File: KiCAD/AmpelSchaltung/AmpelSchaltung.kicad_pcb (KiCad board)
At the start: 2 copper layers, 100 x 100 mm, 31 parts, among them J1 PWR, J2 usb, J3 Conn_01x06_Pin, J5 Conn_01x04_Pin, J6 Conn_01x08_Pin, SW3 SW_SPDT, SW4 SW_SPDT, U1 74HC00, U2 74HC00, U3 AMS1117-3.3

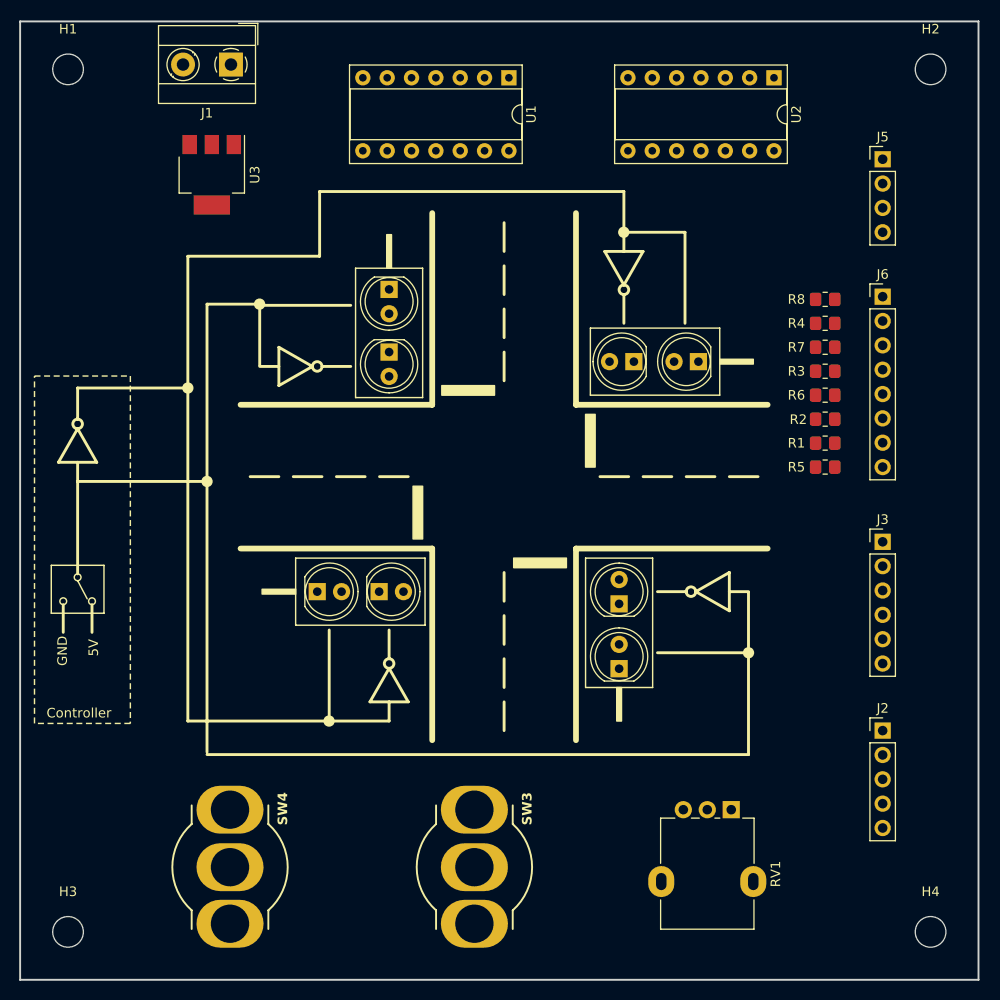
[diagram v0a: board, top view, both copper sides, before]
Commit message: routed ampelschaltung
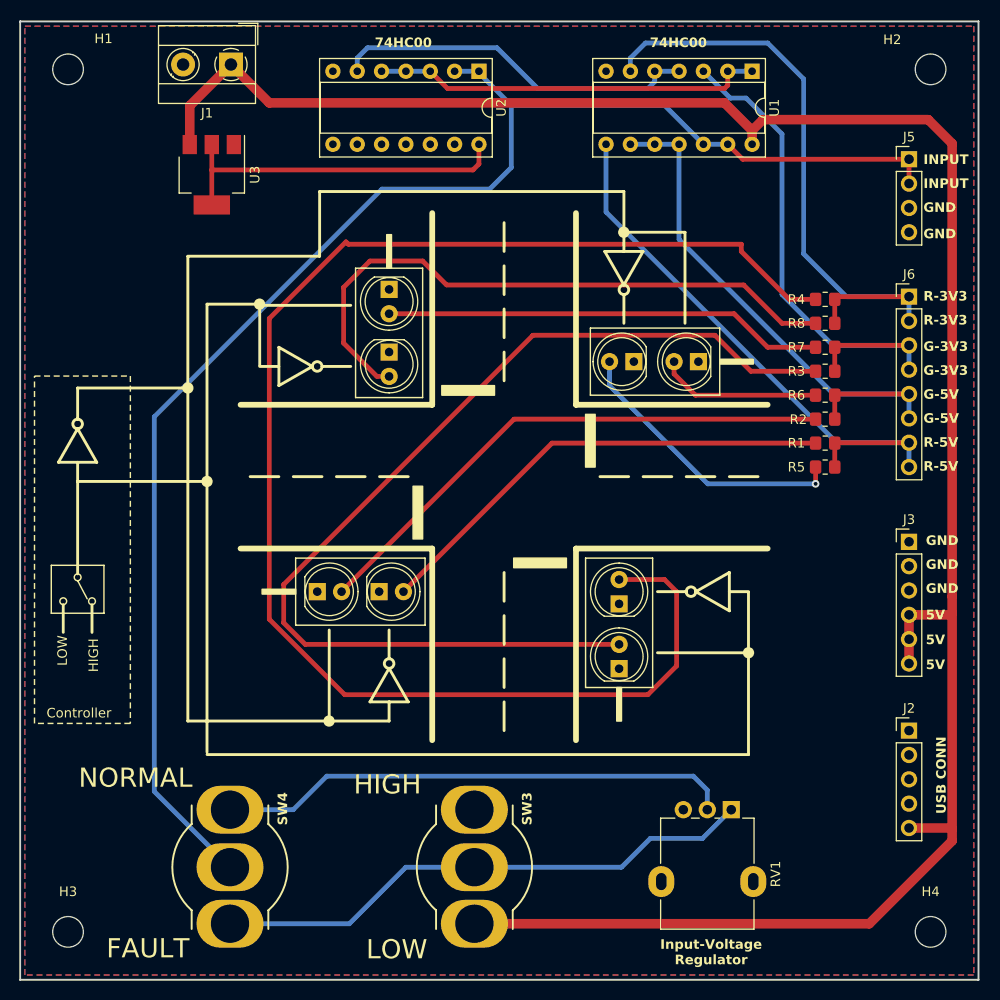
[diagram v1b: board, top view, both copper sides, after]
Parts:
- moved U2 30.8 mm to (145.4, 53.7)
- moved U1 25.4 mm to (173.9, 53.7)
- moved J2 2.75 mm to (190.2, 122.5)
- moved J3 2.75 mm to (190.2, 102.8)
- moved J5 2.75 mm to (190.2, 62.9)
- moved J6 2.75 mm to (190.2, 77.2)
- moved R4 2.50 mm to (181.5, 77.5)
- moved R8 2.50 mm to (181.5, 80.0)
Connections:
- U1 pad 1: Net-(J5-Pin_1) -> Net-(U1-Pad1)
- U1 pad 10: Net-(U1-Pad10) -> Net-(J6-Pin_5)
- U1 pad 11: Net-(J6-Pin_1) -> Net-(J6-Pin_5)
- U1 pad 12: Net-(U1-Pad12) -> Net-(J5-Pin_1)
- U1 pad 13: Net-(U1-Pad12) -> Net-(J5-Pin_1)
- U1 pad 2: Net-(J5-Pin_1) -> Net-(U1-Pad1)
- U1 pad 3: Net-(J6-Pin_5) -> Net-(J6-Pin_3)
- U1 pad 4: Net-(J6-Pin_5) -> Net-(U1-Pad4)
- U1 pad 5: Net-(J6-Pin_5) -> Net-(U1-Pad4)
- U1 pad 6: Net-(J6-Pin_7) -> Net-(J6-Pin_1)
- U1 pad 8: Net-(J6-Pin_3) -> Net-(J6-Pin_7)
- U1 pad 9: Net-(U1-Pad10) -> Net-(J6-Pin_5)
- U2 pad 3: Net-(U1-Pad10) -> Net-(U1-Pad1)
- U2 pad 4: Net-(U1-Pad10) -> Net-(U1-Pad1)
- U2 pad 5: Net-(U1-Pad10) -> Net-(U1-Pad1)
- U2 pad 6: Net-(U1-Pad12) -> Net-(U1-Pad4)
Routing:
- net +5V: track 0.00 -> 231.5 mm
- net Net-(J5-Pin_1): track 0.00 -> 158.7 mm
- net Net-(D4-A): track 0.00 -> 155.9 mm
- net Net-(D3-A): track 0.00 -> 107.8 mm
- net Net-(J6-Pin_1): track 0.00 -> 65.7 mm
- net Net-(D8-A): track 0.00 -> 65.1 mm
- net Net-(J6-Pin_7): track 0.00 -> 61.5 mm
- net Net-(J6-Pin_5): track 0.00 -> 58.6 mm
- net Net-(SW3-B): track 0.00 -> 57.2 mm
- net Net-(D2-A): track 0.00 -> 56.9 mm
- net Net-(J6-Pin_3): track 0.00 -> 56.2 mm
- net Net-(SW4-C): track 0.00 -> 53.9 mm
- net Net-(D1-A): track 0.00 -> 49.4 mm
- net Net-(D7-A): track 0.00 -> 45.9 mm
- net Net-(U1-Pad1): track 0.00 -> 41.0 mm
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- added copper zone on B.Cu, net GND
- added copper zone on F.Cu, net GND
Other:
- board text added: "74HC00"
- board text added: "Ampelschaltung Version: 1.0 Author: Alex Hold"
- board text added: "FAULT"
- board text added: "G-3V3"
- board text added: "G-5V"
- board text added: "HIGH"
- board text added: "INPUT"
- board text added: "Input-Voltage Regulator"
- board text added: "LOW"
- board text added: "NORMAL"
- board text added: "R-3V3"
- board text added: "R-5V"
- board text added: "USB CONN"

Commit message: routed audio controller + added jlc string
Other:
- board text added: "JLCJLCJLCJLC"
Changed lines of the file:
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@@
     (effects (font (size 1 1) (thickness 0.2) bold) (justify left bottom))
+  )
+  (gr_text "JLCJLCJLCJLC" (at 161 58) (layer "F.SilkS")
+    (effects (font (size 1 1) (thickness 0.15)) (justify left bottom))
   )
   (gr_text "HIGH" (at 132.3 129.3) (layer "F.SilkS")
